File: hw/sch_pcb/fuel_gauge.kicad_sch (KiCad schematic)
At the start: 40 parts, among them J10 HEADER_2x01_PARALLEL, J11 HEADER_1x02, Q2 AO3401A, Q3 DMT31M7LPS, Q5 DMT31M7LPS, SW1 SKRTLAE010, SW2 SKRTLAE010, U3 BQ40z50-R2

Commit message: Layout WiP.
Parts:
- C12, C13, C14, C15, C16: footprint Capacitor_SMD:C_0603_1608Metric -> Capacitor_SMD:C_0805_2012Metric
- C17, C18, C21: footprint Capacitor_SMD:C_0402_1005Metric -> Capacitor_SMD:C_0805_2012Metric
- Q3, Q5: footprint Mlab_IO:PowerDI5060-8 -> Mlab_T:D_POWERDI5060-8_6.0x5.1mm_P1.27mm
- R18, R19, R22, R23, R24, R27, R28, R34, R36, TH1, TH2: footprint Resistor_SMD:R_0402_1005Metric -> Resistor_SMD:R_0805_2012Metric
- R35: value 1mR -> 2mR; footprint Resistor_SMD:R_1206_3216Metric -> Resistor_SMD:R_2512_6332Metric; LCSC C76287 -> (none); UST_ID (none) -> 669ba41c6fdfe6f54e2eb51d
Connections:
- net SR+: now reaches C21.1, R34.2, U3.8 (SRP)
- net SR-: now reaches C21.2, R36.2, U3.6 (SRN)
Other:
- note added: "Place to proximity of the switching FETs."
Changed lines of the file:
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@@
 		)
 	)
+	(text "Place to proximity of the switching FETs. "
+		(exclude_from_sim no)
+		(at 181.61 99.06 0)
+		(effects
+			(font
+				(size 1.016 1.016)
+			)
+		)
+	)
 	(label "B+"
 		(at 62.23 101.6 90)
@@
 		)
 	)
+	(label "SR-"
+		(at 85.09 135.89 0)
+		(fields_autoplaced yes)
+		(effects
+			(font
+				(size 1.524 1.524)
+			)
+			(justify left bottom)
+		)
+	)
 	(label "BAT"
 		(at 104.14 85.09 0)
@@
 		)
 	)
+	(label "SR+"
+		(at 74.93 128.27 0)
+		(fields_autoplaced yes)
+		(effects
+			(font
+				(size 1.524 1.524)
+			)
+			(justify left bottom)
+		)
+	)
 	(label "BAT"
 		(at 163.83 93.98 180)
@@
 			)
 		)
-		(property "Footprint" "Mlab_IO:PowerDI5060-8"
+		(property "Footprint" "Mlab_T:D_POWERDI5060-8_6.0x5.1mm_P1.27mm"
 			(at 115.57 63.5 0)
 			(effects
@@
 			)
 		)
-		(property "Footprint" "Resistor_SMD:R_0402_1005Metric"
+		(property "Footprint" "Resistor_SMD:R_0805_2012Metric"
 			(at 153.67 71.12 0)
 			(effects
@@
 			)
 		)
-		(property "Footprint" "Capacitor_SMD:C_0402_1005Metric"
+		(property "Footprint" "Capacitor_SMD:C_0805_2012Metric"
 			(at 74.93 132.08 0)
 			(effects
@@
 			)
 		)
-		(property "Footprint" "Capacitor_SMD:C_0603_1608Metric"
+		(property "Footprint" "Capacitor_SMD:C_0805_2012Metric"
 			(at 120.65 40.64 0)
 			(effects
@@
 			)
 		)
-		(property "Footprint" "Resistor_SMD:R_0402_1005Metric"
+		(property "Footprint" "Resistor_SMD:R_0805_2012Metric"
 			(at 68.58 128.27 0)
 			(effects
@@
 			)
 		)
-		(property "Footprint" "Resistor_SMD:R_0402_1005Metric"
+		(property "Footprint" "Resistor_SMD:R_0805_2012Metric"
 			(at 113.03 78.74 0)
 			(effects
@@
 			)
 		)
-		(property "Footprint" "Capacitor_SMD:C_0603_1608Metric"
+		(property "Footprint" "Capacitor_SMD:C_0805_2012Metric"
 			(at 161.29 71.12 0)
 			(effects
@@
 			)
 		)
-		(property "Footprint" "Mlab_IO:PowerDI5060-8"
+		(property "Footprint" "Mlab_T:D_POWERDI5060-8_6.0x5.1mm_P1.27mm"
 			(at 135.89 63.5 0)
 			(effects
@@
 			)
 		)
-		(property "Footprint" "Capacitor_SMD:C_0603_1608Metric"
+		(property "Footprint" "Capacitor_SMD:C_0805_2012Metric"
 			(at 161.29 77.47 0)
 			(effects
@@
 			)
 		)
-		(property "Footprint" "Resistor_SMD:R_0402_1005Metric"
+		(property "Footprint" "Resistor_SMD:R_0805_2012Metric"
 			(at 106.68 71.12 0)
 			(effects
@@
 			)
 		)
-		(property "Footprint" "Capacitor_SMD:C_0603_1608Metric"
+		(property "Footprint" "Capacitor_SMD:C_0805_2012Metric"
 			(at 95.25 96.52 0)
 			(effects
@@
 			)
 		)
-		(property "Footprint" "Capacitor_SMD:C_0402_1005Metric"
+		(property "Footprint" "Capacitor_SMD:C_0805_2012Metric"
 			(at 82.55 114.3 0)
 			(effects
@@
 			)
 		)
-		(property "Footprint" "Resistor_SMD:R_0402_1005Metric"
+		(property "Footprint" "Resistor_SMD:R_0805_2012Metric"
 			(at 123.19 148.59 0)
 			(effects
@@
 			)
 		)
-		(property "Footprint" "Capacitor_SMD:C_0603_1608Metric"
+		(property "Footprint" "Capacitor_SMD:C_0805_2012Metric"
 			(at 133.35 40.64 0)
 			(effects
@@
 			)
 		)
-		(property "Footprint" "Resistor_SMD:R_0402_1005Metric"
+		(property "Footprint" "Resistor_SMD:R_0805_2012Metric"
 			(at 68.58 135.89 0)
 			(effects
@@
 			)
 		)
-		(property "Footprint" "Resistor_SMD:R_0402_1005Metric"
+		(property "Footprint" "Resistor_SMD:R_0805_2012Metric"
 			(at 119.38 62.23 0)
 			(effects
@@
 			)
 		)
-		(property "Footprint" "Resistor_SMD:R_0402_1005Metric"
+		(property "Footprint" "Resistor_SMD:R_0805_2012Metric"
 			(at 127 54.61 0)
 			(effects
@@
 		(fields_autoplaced yes)
 		(property "Reference" "R35"
-			(at 63.7286 131.2453 0)
+			(at 63.7286 130.8678 0)
 			(effects
 				(font
@@
 			)
 		)
-		(property "Value" "1mR"
-			(at 63.7286 133.7822 0)
+		(property "Value" "2mR"
+			(at 63.7286 133.2921 0)
 			(effects
 				(font
@@
 			)
 		)
-		(property "Footprint" "Resistor_SMD:R_1206_3216Metric"
+		(property "Footprint" "Resistor_SMD:R_2512_6332Metric"
 			(at 62.23 132.08 0)
 			(effects
@@
 			)
 		)
-		(property "Datasheet" "~"
+		(property "Datasheet" "https://www.tme.eu/Document/9eb17c5caf6d68fb7c80b751e0adae3a/LR12.pdf"
 			(at 62.23 132.08 0)
 			(effects
@@
 			)
 		)
-		(property "LCSC" "C76287"
+		(property "UST_ID" "669ba41c6fdfe6f54e2eb51d"
 			(at 62.23 132.08 0)
 			(effects
@@
 			)
 		)
-		(property "Footprint" "Resistor_SMD:R_0402_1005Metric"
+		(property "Footprint" "Resistor_SMD:R_0805_2012Metric"
 			(at 113.03 148.59 0)
 			(effects
@@
 			)
 		)
-		(property "Footprint" "Resistor_SMD:R_0402_1005Metric"
+		(property "Footprint" "Resistor_SMD:R_0805_2012Metric"
 			(at 144.78 71.12 0)
 			(effects
@@
 			)
 		)
-		(property "Footprint" "Capacitor_SMD:C_0402_1005Metric"
+		(property "Footprint" "Capacitor_SMD:C_0805_2012Metric"
 			(at 82.55 106.68 0)
 			(effects
@@
 			)
 		)
-		(property "Footprint" "Resistor_SMD:R_0402_1005Metric"
+		(property "Footprint" "Resistor_SMD:R_0805_2012Metric"
 			(at 128.27 74.93 0)
 			(effects

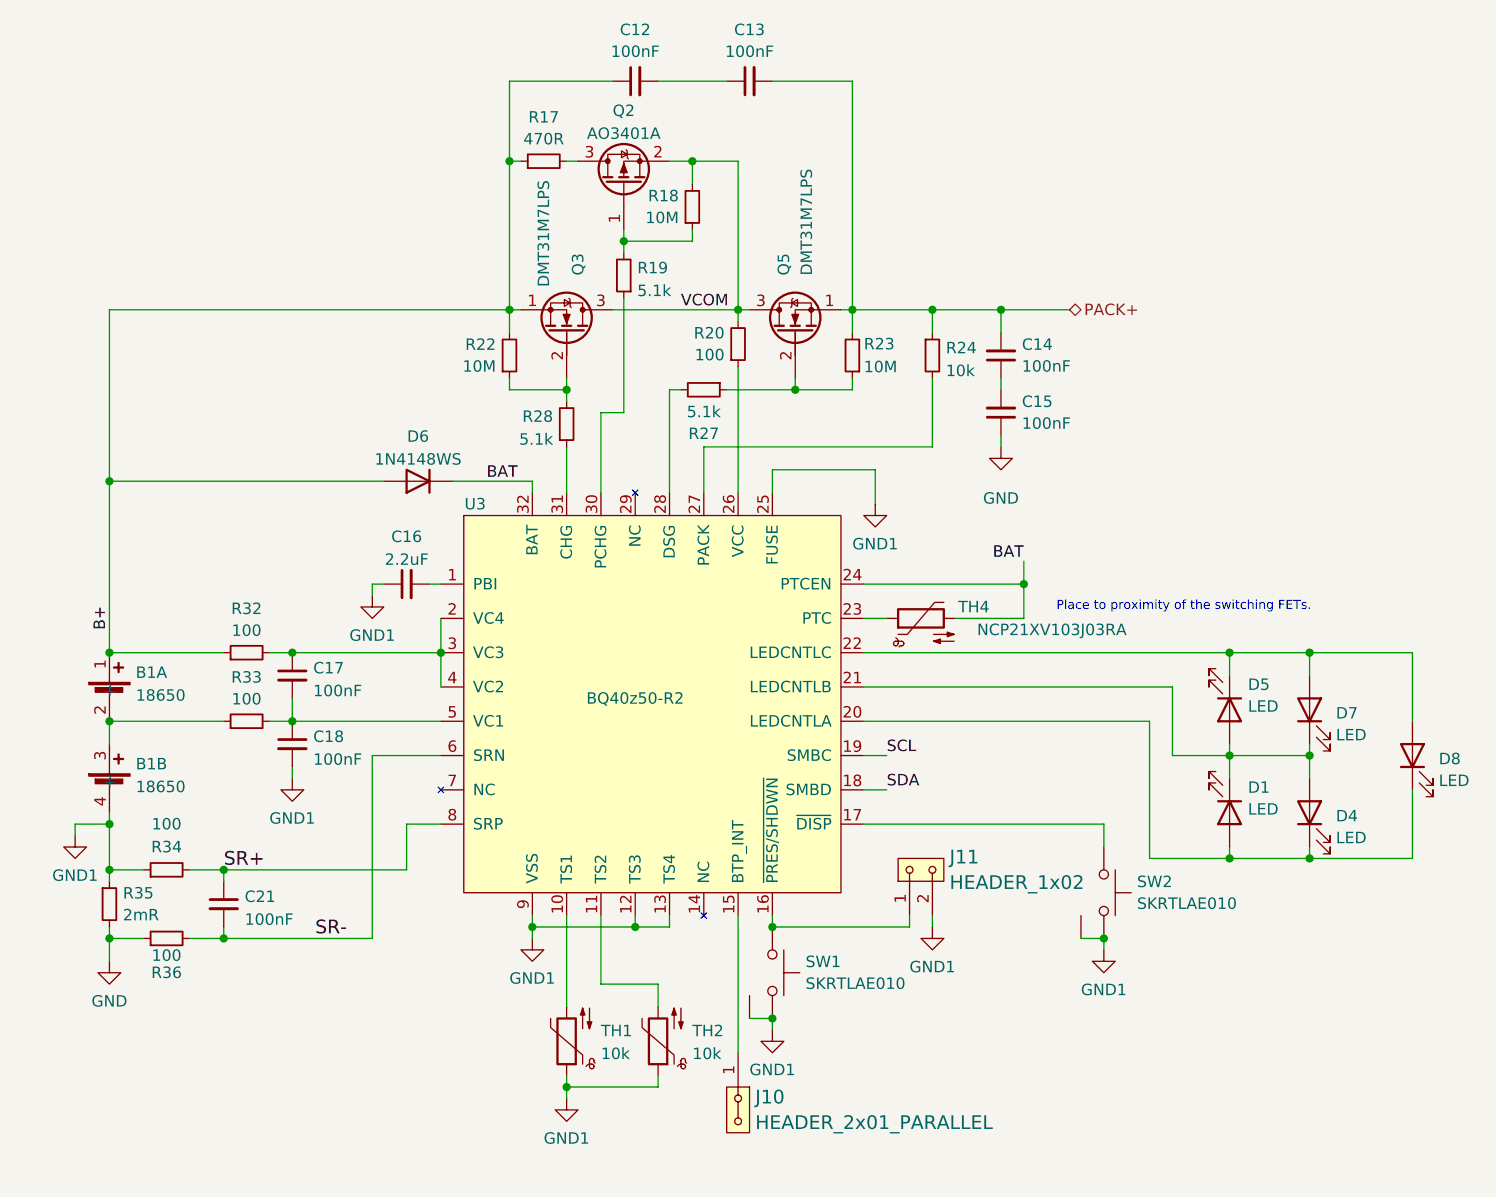
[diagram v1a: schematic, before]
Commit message: Partially routed PCB.
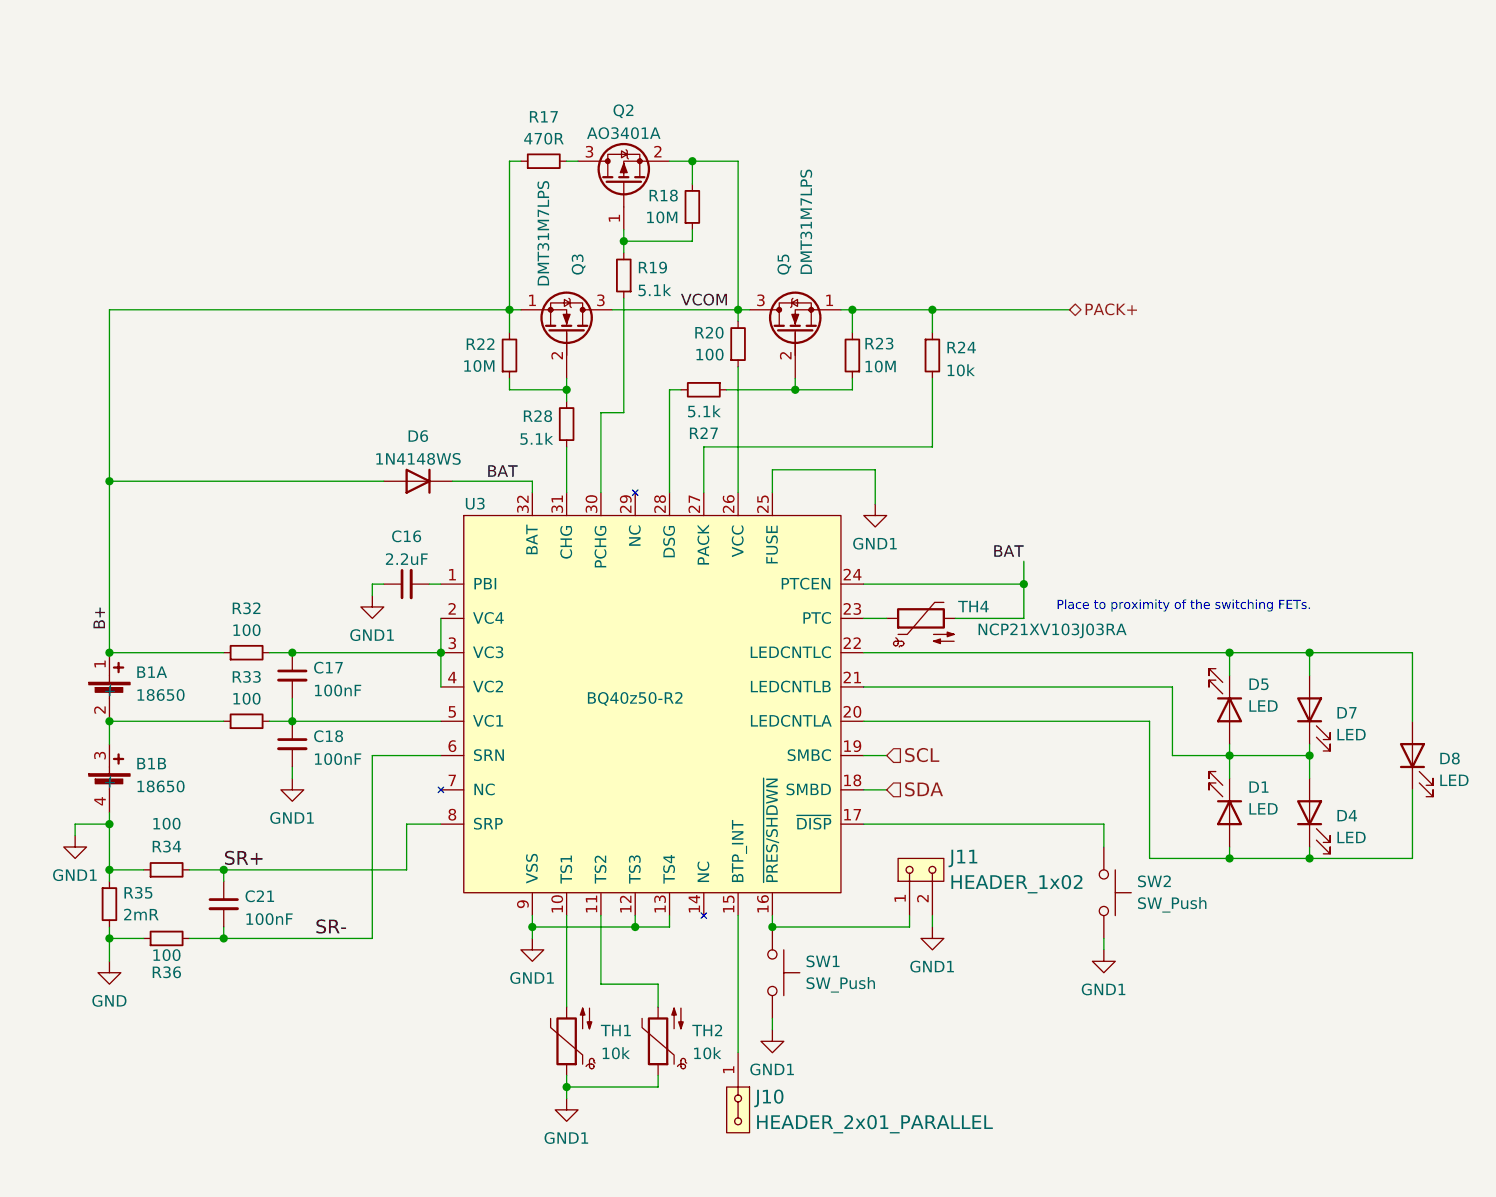
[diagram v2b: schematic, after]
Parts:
- removed C12, C13, C14, C15: 100nF, Capacitor_SMD:C_0805_2012Metric, symbol Device:C_Small
- removed SW1, SW2: SKRTLAE010, Mlab_SW:SKRT, symbol MLAB_SW:SW_Push_shield
- added SW1, SW2: SW_Push, Mlab_SW:SW_PUSH_SMALL, symbol Switch:SW_Push
- D6: footprint Diode_SMD:D_SOD-323 -> Diode_SMD:D_0805_2012Metric; LCSC C2128 -> (none); UST_ID (none) -> 5c70984512875079b91f88c5
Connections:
- net GND1: now also SW1.2, SW2.2
- net at J11.1, U3.16 (~{PRES/SHDWN}): now also SW1.1
- net at U3.17 (~{DISP}): now also SW2.1

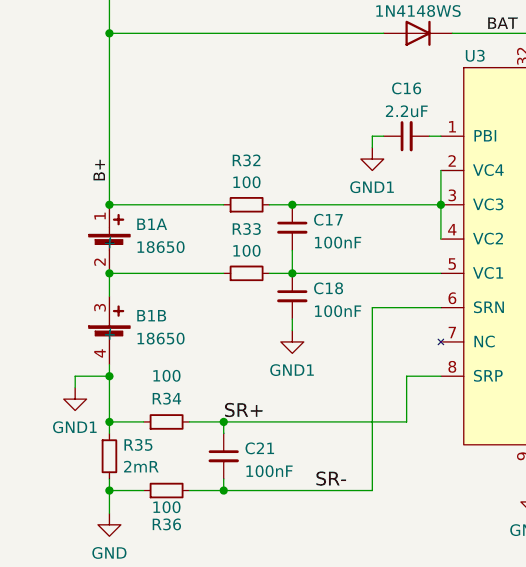
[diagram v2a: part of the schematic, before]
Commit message: Routed few aditional nets Battery mid-point zone connection changed to a track with special net class.
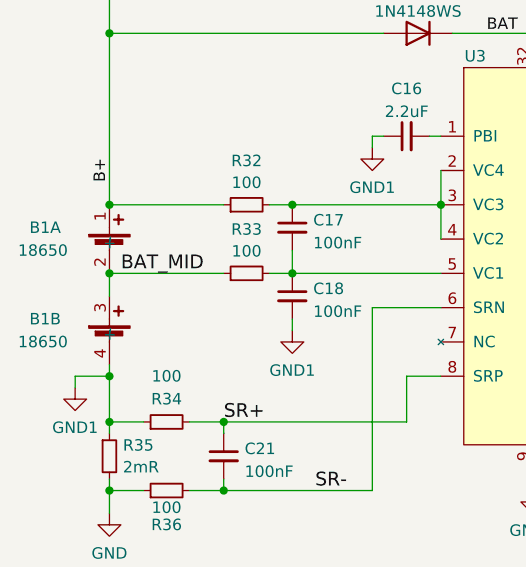
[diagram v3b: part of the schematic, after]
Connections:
- net BAT_MID: now reaches B1.2 (-), B1.3 (+), R33.1
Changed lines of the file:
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@@
+		)
+	)
+	(label "BAT_MID"
+		(at 63.5 111.76 0)
+		(fields_autoplaced yes)
+		(effects
+			(font
+				(size 1.524 1.524)
+			)
+			(justify left bottom)
 		)
 	)
@@
 		)
 	)
+	(netclass_flag ""
+		(length 2.54)
+		(shape round)
+		(at 66.04 111.76 180)
+		(fields_autoplaced yes)
+		(effects
+			(font
+				(size 1.524 1.524)
+			)
+			(justify right bottom)
+		)
+		(property "Netclass" "BAT_MID"
+			(at 67.0052 114.3 0)
+			(effects
+				(font
+					(size 1.27 1.27)
+					(italic yes)
+				)
+				(justify left)
+			)
+		)
+	)
 	(symbol
 		(lib_id "Device:Q_NMOS_SGD")
@@
 		(on_board yes)
 		(dnp no)
-		(fields_autoplaced yes)
 		(property "Reference" "B1"
-			(at 65.151 116.5133 0)
+			(at 53.34 116.84 0)
 			(effects
 				(font
@@
 		)
 		(property "Value" "18650"
-			(at 65.151 119.0502 0)
+			(at 52.07 119.38 0)
 			(effects
 				(font
@@
 		(on_board yes)
 		(dnp no)
-		(fields_autoplaced yes)
 		(property "Reference" "B1"
-			(at 65.151 106.3533 0)
+			(at 53.34 106.68 0)
 			(effects
 				(font
@@
 		)
 		(property "Value" "18650"
-			(at 65.151 108.8902 0)
-			(effects
-				(font
+			(at 52.07 109.22 0)
+			(effects
+				(font

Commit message: Routed another tracks.
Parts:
- Q2: value AO3401A -> AP2305AGN-HF-3; LCSC C15127 -> (none); UST_ID (none) -> 5c70984712875079b91f8af1
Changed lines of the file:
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@@
 		(on_board yes)
 		(dnp no)
-		(fields_autoplaced yes)
 		(property "Reference" "Q2"
 			(at 119.38 43.9252 90)
@@
 			)
 		)
-		(property "Value" "AO3401A"
-			(at 119.38 46.4621 90)
+		(property "Value" "AP2305AGN-HF-3"
+			(at 121.92 41.91 90)
 			(effects
 				(font
@@
 			)
 		)
-		(property "Datasheet" "http://www.aosmd.com/pdfs/datasheet/AO3401A.pdf"
+		(property "Datasheet" "https://www.tme.eu/Document/fc64476bcfec1f3af35a324c08c5f351/AP2305AGN-3.pdf"
 			(at 119.38 52.07 0)
 			(effects
@@
 			)
 		)
-		(property "LCSC" "C15127"
-			(at 119.38 52.07 90)
+		(property "UST_ID" "5c70984712875079b91f8af1"
+			(at 119.38 52.07 0)
 			(effects
 				(font
